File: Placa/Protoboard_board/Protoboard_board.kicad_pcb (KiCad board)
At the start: 2 copper layers, 40.7 x 40.9 mm, 4 parts, among them J1 Conn_02x05_Counter_Clockwise, J2 Right_Conector, J3 Left_Conector, U1 CH32V003FxPx

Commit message: Função do PWM
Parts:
- moved J2 13.2 mm to (54.7, 39.2)
- moved J1 7.57 mm to (39.8, 36.4)
- moved U1 7.57 mm to (45.9, 51.6)
- moved J3 0.70 mm to (36.3, 39.0)
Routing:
- net /PA2: track 13.8 -> 6.80 mm
- net /PA1: track 14.6 -> 7.58 mm
- net /5V_linker: track 32.9 -> 26.1 mm
- net GND: track 35.2 -> 28.4 mm
- net /PD0: track 15.0 -> 8.15 mm
- net /PD7: track 15.4 -> 8.69 mm
- net /PC0: track 16.8 -> 10.6 mm
- net /PC3: track 13.2 -> 7.46 mm
- net /PC4: track 12.4 -> 6.68 mm
- net /PC5: track 11.6 -> 5.99 mm
- net /PC7: track 13.1 -> 7.56 mm
- net /PC6: track 12.3 -> 6.78 mm
- net /PD6: track 31.1 -> 25.5 mm
- net /PC2: track 14.0 -> 8.60 mm
- net /PC1: track 14.7 -> 9.91 mm
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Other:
- board size 40.7 x 40.9 mm -> 25.4 x 40.9 mm

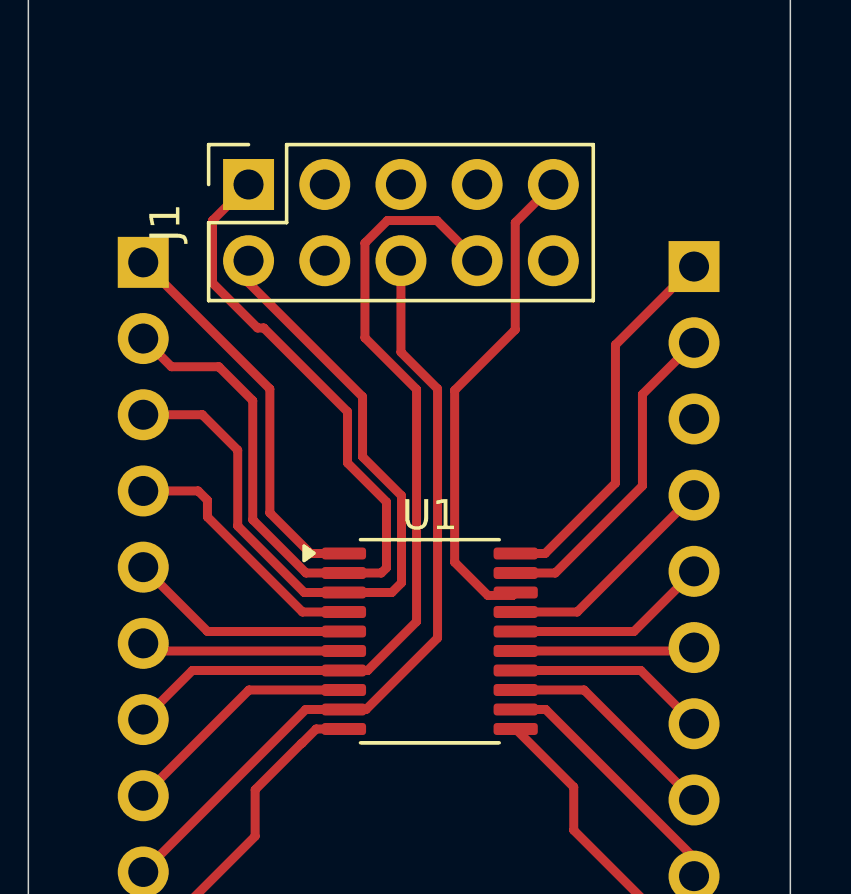
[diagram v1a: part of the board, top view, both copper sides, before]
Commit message: Driver do Timer1 e as funções do som e handler de erro
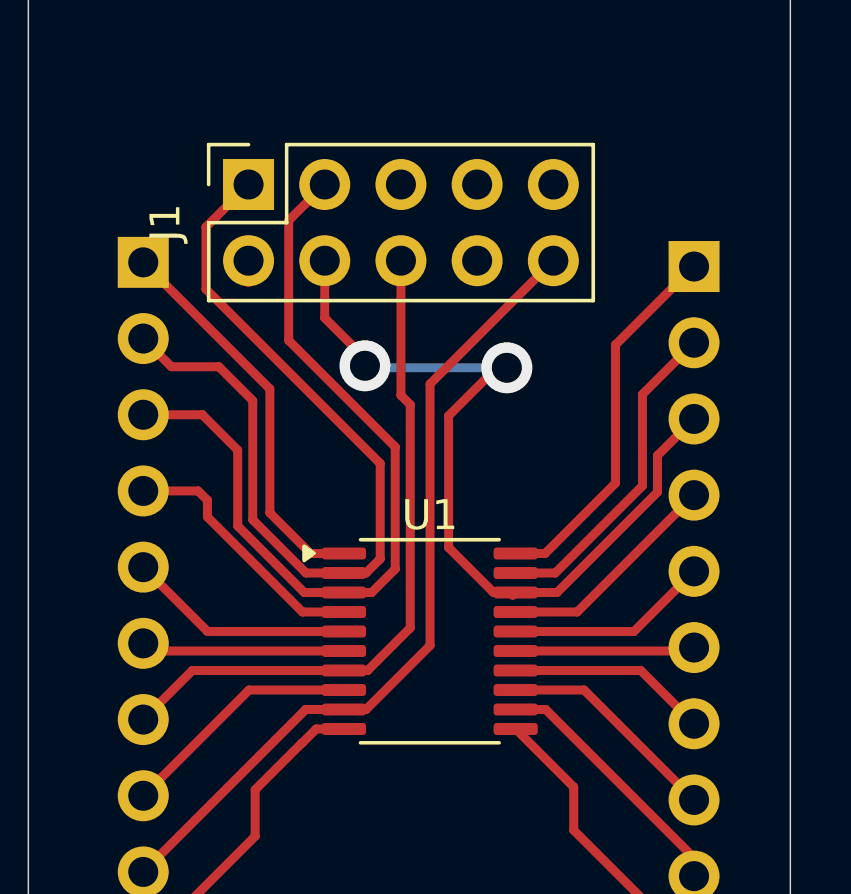
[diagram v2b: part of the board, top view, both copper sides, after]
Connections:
- J1 pad 10: /SWCLK_linker -> /5V_linker
- J1 pad 2: /PD6 -> /SWCLK_linker
- J1 pad 3: unconnected-(J1-Pin_3-Pad3) -> /PD6
- J1 pad 4: unconnected-(J1-Pin_4-Pad4) -> /SWDIO_linker
- J1 pad 6: /5V_linker -> GND
- J1 pad 7: /3V3_linker -> unconnected-(J1-Pin_7-Pad7)
- J1 pad 8: GND -> /3V3_linker
- J1 pad 9: /SWDIO_linker -> unconnected-(J1-Pin_9-Pad9)
- J2 pad 3: unconnected-(J2-Pin_3-Pad3) -> /SWDIO_linker
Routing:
- net /SWDIO_linker: track 16.5 -> 27.9 mm, vias 0 -> 2
- net GND: track 28.4 -> 22.5 mm
- net /PD6: track 25.5 -> 27.4 mm
- net /5V_linker: track 26.1 -> 27.2 mm
- net /SWCLK_linker: track 0.00 -> 0.73 mm
